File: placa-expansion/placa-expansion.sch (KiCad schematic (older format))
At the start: 17 parts, among them J1 PBD-26, P1 BATT, P2 CONN_3PI, P3 PWR_HUB, P4 PWR_3pi, P5 CONN_4, P6 CONN_4, P7 CONN_4, P8 CONN_4, U1 PTN78020

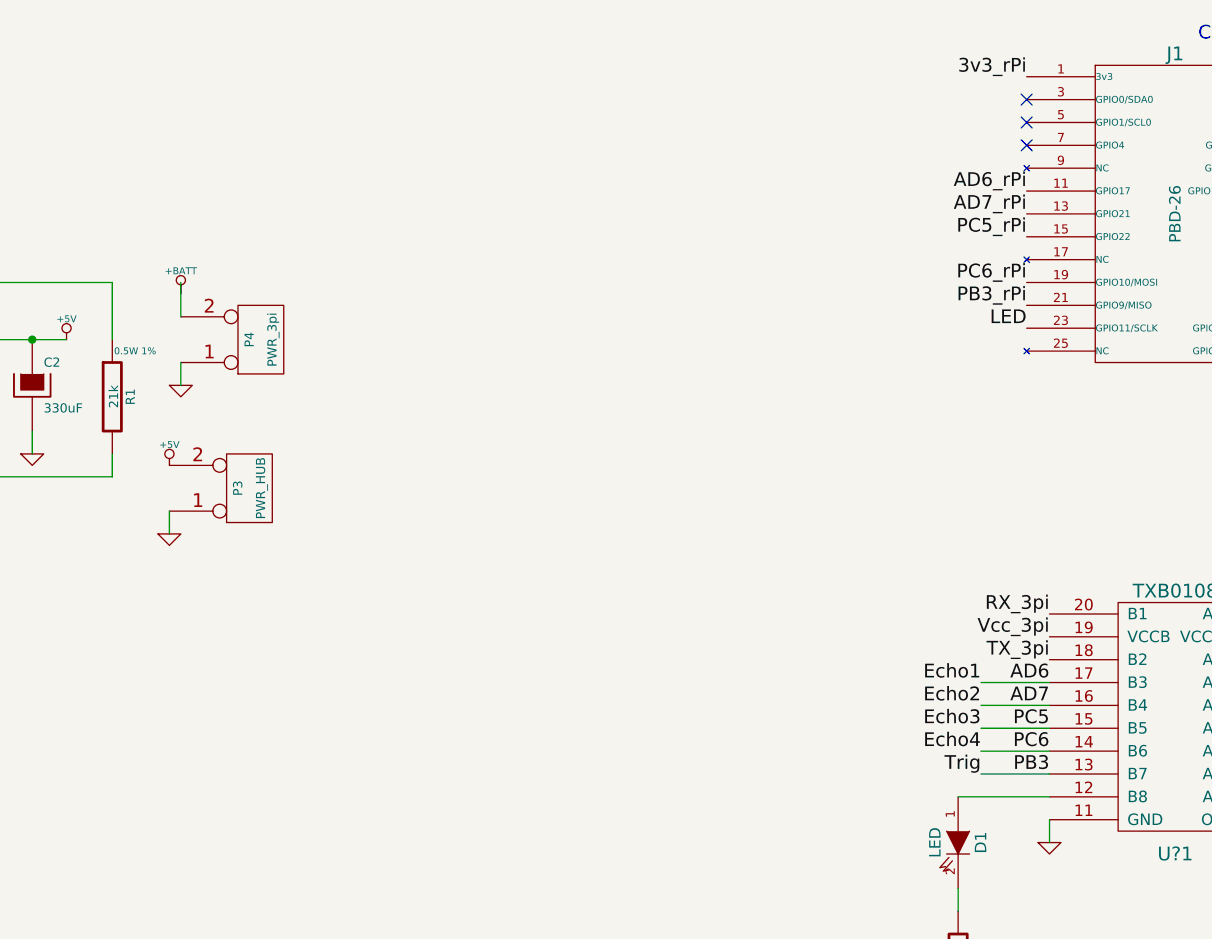
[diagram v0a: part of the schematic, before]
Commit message: Comienzamos a rutear la placa interfaz
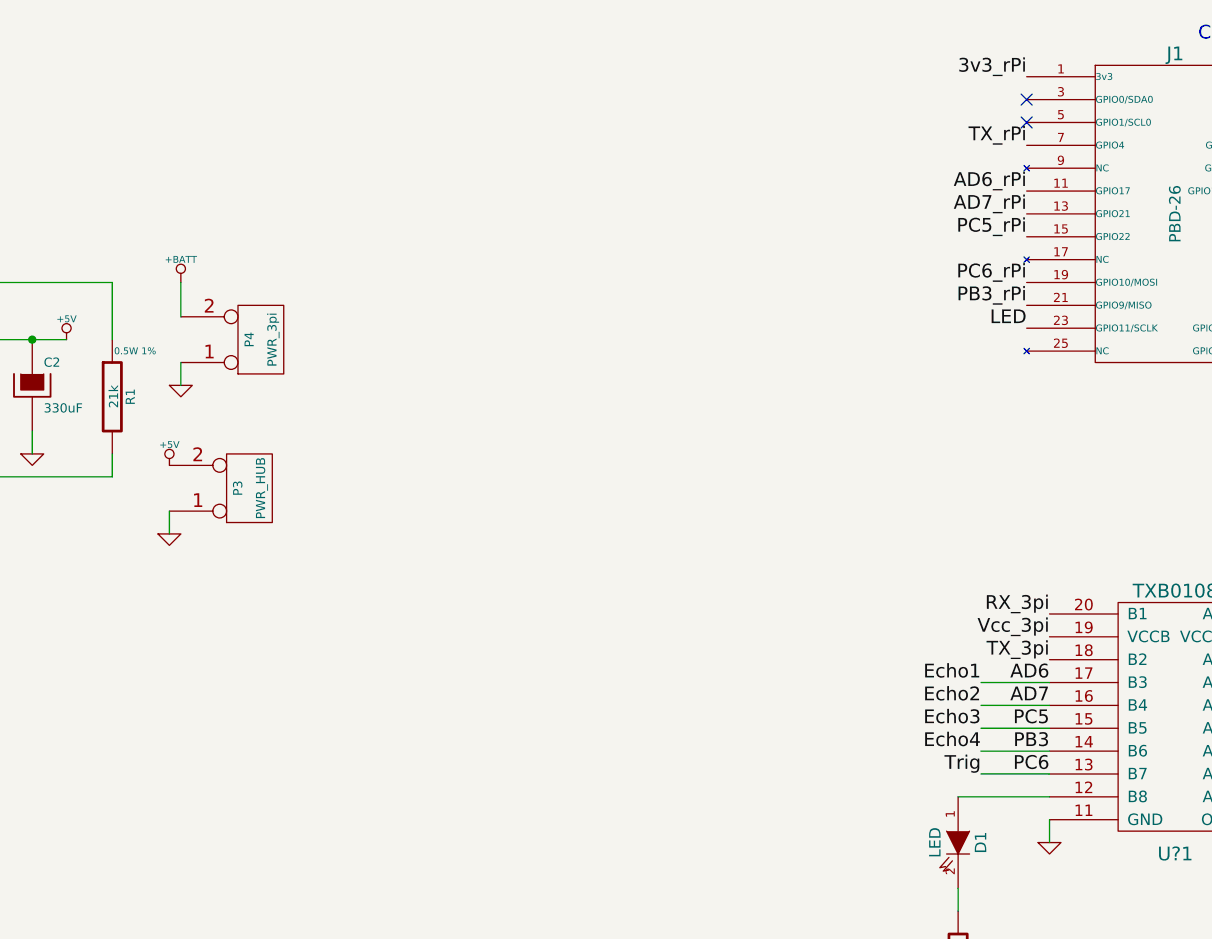
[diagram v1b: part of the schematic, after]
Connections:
- no-connect marks 10 -> 9
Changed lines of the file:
@@
-EESchema Schematic File Version 2  date vie 17 may 2013 21:18:23 ART
+EESchema Schematic File Version 2  date vie 31 may 2013 21:32:53 ART
 LIBS:power
 LIBS:device
@@
 LIBS:txb0108
 LIBS:ptn78020
+LIBS:placa-expansion-cache
 EELAYER 27 0
 EELAYER END
@@
 Sheet 1 1
 Title "Expansión para el 3pi - Raspberry Pi"
-Date "17 may 2013"
+Date "1 jun 2013"
 Rev "0.8"
 Comp "Club de Robótica FIUBA"
@@
 L +BATT #PWR010
 U 1 1 517B1D19
-P 4850 2300
-F 0 "#PWR010" H 4850 2250 20  0001 C CNN
-F 1 "+BATT" H 4850 2400 30  0000 C CNN
-F 2 "" H 4850 2300 60  0000 C CNN
-F 3 "" H 4850 2300 60  0000 C CNN
-	1    4850 2300
+P 4850 2250
+F 0 "#PWR010" H 4850 2200 20  0001 C CNN
+F 1 "+BATT" H 4850 2350 30  0000 C CNN
+F 2 "" H 4850 2250 60  0000 C CNN
+F 3 "" H 4850 2250 60  0000 C CNN
+	1    4850 2250
 	1    0    0    -1
 $EndComp
@@
 Text Label 8650 4200 2    60   ~ 0
 PC5
+Text Label 8650 4400 2    60   ~ 0
+PC6
 Text Label 8650 4300 2    60   ~ 0
-PC6
-Text Label 8650 4400 2    60   ~ 0
 PB3
 $Comp
@@
 NoConn ~ 8550 1450
 NoConn ~ 8550 1550
-NoConn ~ 8550 1650
 NoConn ~ 9850 2550
 NoConn ~ 9850 2450
@@
 Wire Wire Line
 	8350 4000 8650 4000
+Text Label 8550 1650 2    60   ~ 0
+TX_rPi
 $EndSCHEMATC

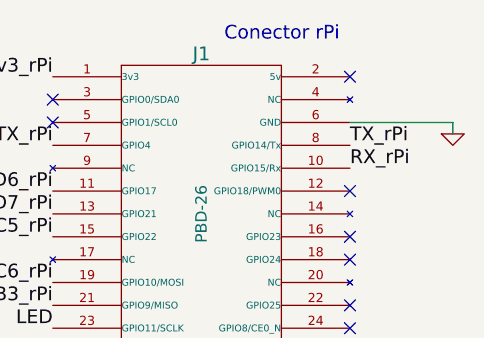
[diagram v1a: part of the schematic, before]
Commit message: Borro las pistas y agrando los pads.
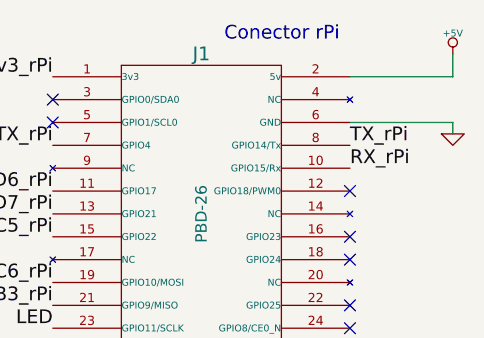
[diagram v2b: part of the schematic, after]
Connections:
- wire segments 52 -> 54
- no-connect marks 9 -> 8
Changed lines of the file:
@@
-EESchema Schematic File Version 2  date vie 31 may 2013 21:32:53 ART
+EESchema Schematic File Version 2  date vie 27 sep 2013 20:42:12 ART
 LIBS:power
 LIBS:device
@@
 LIBS:txb0108
 LIBS:ptn78020
-LIBS:placa-expansion-cache
 EELAYER 27 0
 EELAYER END
@@
 Sheet 1 1
 Title "Expansión para el 3pi - Raspberry Pi"
-Date "1 jun 2013"
+Date "27 sep 2013"
 Rev "0.8"
 Comp "Club de Robótica FIUBA"
@@
 	1    0    0    -1
 $EndComp
-NoConn ~ 9850 1350
 Text Label 3550 4900 0    60   ~ 0
 Vcc_3pi
@@
 Text Label 8650 3800 2    60   ~ 0
 Vcc_3pi
-$Comp
-L PBD-26 J1
-U 1 1 5173EFB3
-P 9200 1950
-F 0 "J1" H 9200 2650 60  0000 C CNN
-F 1 "PBD-26" V 9200 1950 50  0000 C CNN
-F 2 "" H 9200 1950 60  0001 C CNN
-F 3 "" H 9200 1950 60  0001 C CNN
-	1    9200 1950
-	1    0    0    -1
-$EndComp
 Text Label 8550 1350 2    60   ~ 0
 3v3_rPi
@@
 Text Label 8550 1650 2    60   ~ 0
 TX_rPi
+$Comp
+L PBD-26 J1
+U 1 1 5173EFB3
+P 9200 1950
+F 0 "J1" H 9200 2650 60  0000 C CNN
+F 1 "PBD-26" V 9200 1950 50  0000 C CNN
+F 2 "" H 9200 1950 60  0001 C CNN
+F 3 "" H 9200 1950 60  0001 C CNN
+	1    9200 1950
+	1    0    0    -1
+$EndComp
+Wire Wire Line
+	9850 1350 10300 1350
+$Comp
+L +5V #PWR028
+U 1 1 5246193B
+P 10300 1250
+F 0 "#PWR028" H 10300 1340 20  0001 C CNN
+F 1 "+5V" H 10300 1340 30  0000 C CNN
+F 2 "" H 10300 1250 60  0000 C CNN
+F 3 "" H 10300 1250 60  0000 C CNN
+	1    10300 1250
+	1    0    0    -1
+$EndComp
+Wire Wire Line
+	10300 1350 10300 1250
 $EndSCHEMATC
